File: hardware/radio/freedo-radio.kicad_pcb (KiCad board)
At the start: 4 copper layers, 92 x 60 mm, 146 parts, among them J1 SMA-KE-347-H13.5-1.6, J201 TYPE-C-31-M-12, J202 UART0, J301 DS1128-S80BP, SW201 TS-1187A-B-A-B, SW202 TS-1187A-B-A-B, T301 B1608S, U1 CC1101RGPR, U201 ESP32-S3-MINI-1-N8, U202 USBLC6-2SC6, U203 LDL1117S33R, U301 W5500, U401 DP9900LP-5V, X1 X322526MMB4SI, Y301 X322525MOB4SI

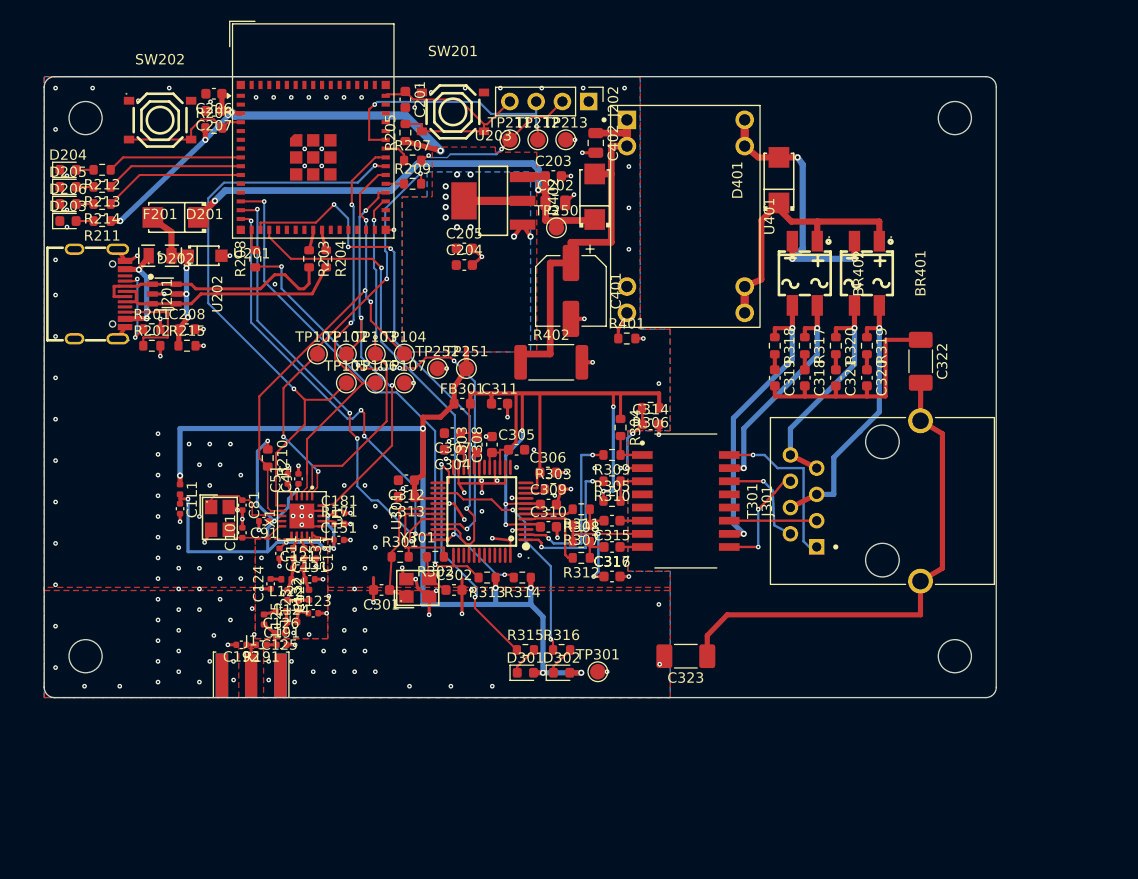
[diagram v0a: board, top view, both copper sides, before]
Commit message: fix(hardware): apply the pcb review fixes and align the usb-c to the edge
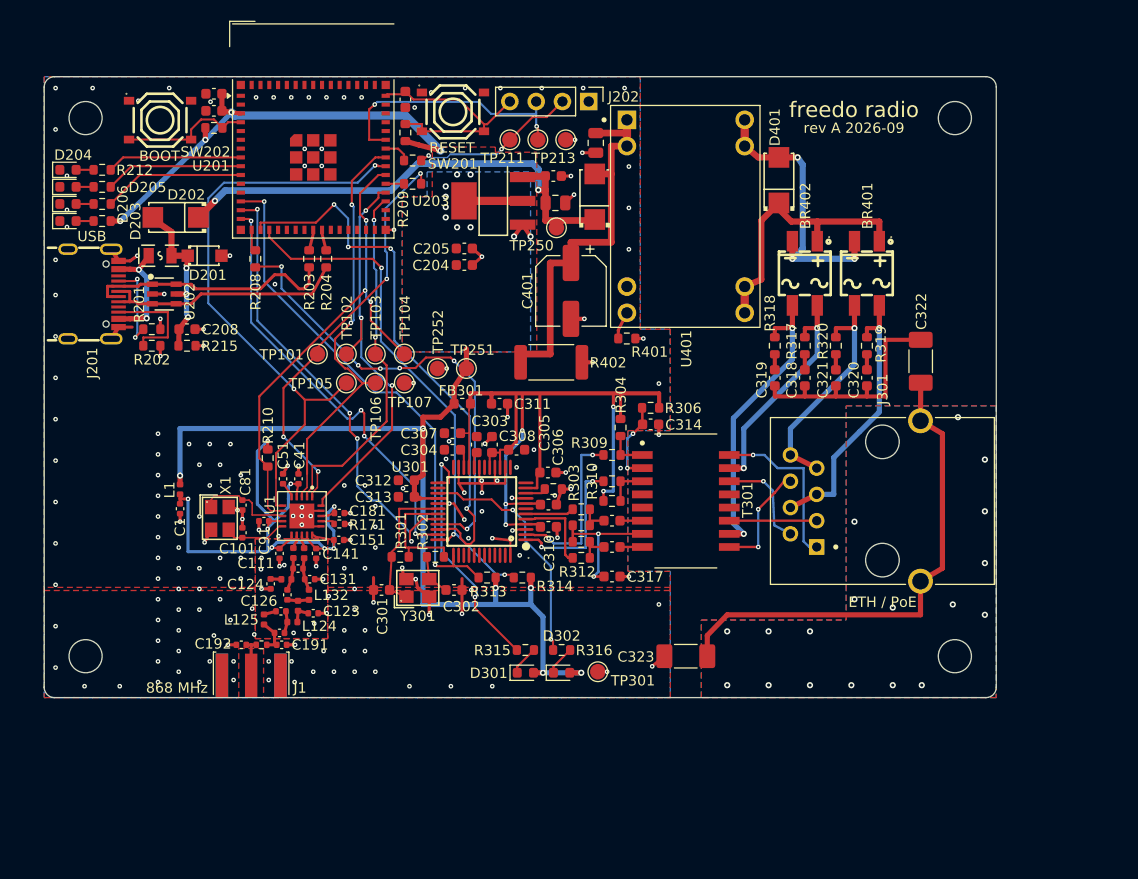
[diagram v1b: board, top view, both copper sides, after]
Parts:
- moved J201 0.63 mm to (194.8, 71.0)
- moved C51 0.45 mm to (213.1, 88.9)
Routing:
- net /rf/3V3_RF: track 52.3 -> 56.7 mm
- net GND: track 73.9 -> 78.0 mm, vias 197 -> 200
- net Net-(F201-Pad1): track 9.11 -> 10.4 mm
- net /usb_power/USB_DP: track 22.6 -> 23.2 mm
- net /usb_power/CC2: track 8.87 -> 9.50 mm
- net /usb_power/CC1: track 7.58 -> 8.21 mm
- net /usb_power/USB_DN: track 22.6 -> 23.2 mm
- net /ethernet_poe/SHIELD: vias 0 -> 18
- added copper zone on B.Cu, net /ethernet_poe/SHIELD
- added copper zone on F.Cu, net /ethernet_poe/SHIELD
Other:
- board text added: "868 MHz"
- board text added: "BOOT"
- board text added: "ETH / PoE"
- board text added: "RESET"
- board text added: "USB"
- board text added: "freedo radio"
- board text added: "rev A 2026-09"

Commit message: feat(hardware): re-place the board with rework spacing
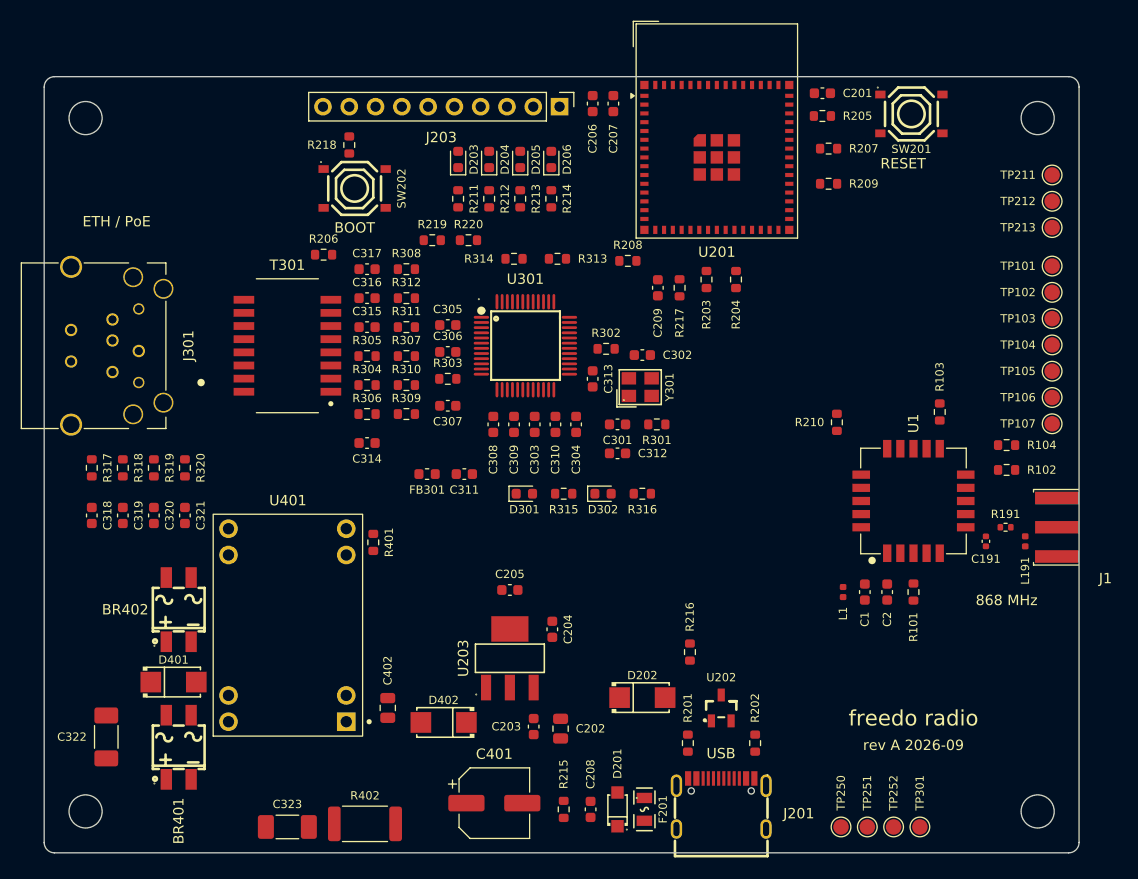
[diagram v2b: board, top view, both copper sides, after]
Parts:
- removed C101, C81: 15pF, freedo-radio:C_0402_1005Metric
- removed C111, C141, C151, C181, C41, C51, C91: 100nF, freedo-radio:C_0402_1005Metric
- removed C121: 1pF, freedo-radio:C_0402_1005Metric
- removed C122, C131: 1.5pF, freedo-radio:C_0402_1005Metric
- removed C123: 3.3pF, freedo-radio:C_0402_1005Metric
- removed C124: 100pF, freedo-radio:C_0402_1005Metric
- removed C125: 12pF, freedo-radio:C_0402_1005Metric
- removed C126: 47pF, freedo-radio:C_0402_1005Metric
- removed C192: DNP, freedo-radio:C_0402_1005Metric
- removed J202: UART0, freedo-radio:PinHeader_1x04_P2.54mm_Vertical
- removed L121, L123, L124, L131: 12nH, freedo-radio:L_0402_1005Metric
- removed L122, L132: 18nH, freedo-radio:L_0402_1005Metric
- removed L125: 3.3nH, freedo-radio:L_0402_1005Metric
- removed R171: 56k, freedo-radio:R_0402_1005Metric
- removed X1: X322526MMB4SI, freedo-radio:CRYSTAL-SMD_4P-L3.2-W2.5-BL
- added C2: 100nF, freedo-radio:C_0603_1608Metric, F.Cu at (271.5, 99.8)
- added C209: 100nF, freedo-radio:C_0603_1608Metric, F.Cu at (249.3, 70.4)
- added J203: GPIO, freedo-radio:PinHeader_1x10_P2.54mm_Vertical, F.Cu at (239.8, 52.9)
- added L191: 56nH, freedo-radio:L_0402_1005Metric, F.Cu at (284.8, 94.9)
- added R101: 0R, freedo-radio:R_0603_1608Metric, F.Cu at (274.0, 99.8)
- added R102: 0R, freedo-radio:R_0603_1608Metric, F.Cu at (283.0, 88.0)
- added R103: 0R, freedo-radio:R_0603_1608Metric, F.Cu at (276.5, 82.4)
- added R104: 0R, freedo-radio:R_0603_1608Metric, F.Cu at (283.0, 85.6)
- added R216: 68k, freedo-radio:R_0603_1608Metric, F.Cu at (252.4, 105.6)
- added R217: 100k, freedo-radio:R_0603_1608Metric, F.Cu at (251.4, 70.4)
- added R218: 1k, freedo-radio:R_0603_1608Metric, F.Cu at (219.5, 56.6)
- added R219: 4.7k, freedo-radio:R_0603_1608Metric, F.Cu at (227.5, 65.8)
- added R220: 4.7k, freedo-radio:R_0603_1608Metric, F.Cu at (231.0, 65.8)
- C1: value 1uF -> 10uF; footprint freedo-radio:C_0402_1005Metric -> freedo-radio:C_0603_1608Metric
- C202: value 22uF -> 10uF
- D201: value SMF5.0A -> SMF6.0A
- J301: value DS1128-S80BP -> TM24RSG-5A-88; footprint freedo-radio:RJ45_CONNFLY_DS1128-S80BP -> freedo-radio:RJ45_Hirose_TM24RSG-5A-88
- R207: value 510R -> 1k
- R215: value 10k -> 4.7k
- U1: value CC1101RGPR -> E07-900MM10S; footprint freedo-radio:QFN-20-1EP_4x4mm_P0.5mm_EP2.4x2.4mm_TI_RGP0020H -> freedo-radio:Ebyte_LCC-20_10x10mm_P1.27mm_E07-MM10S_E22-MM22S
- U202: value USBLC6-2SC6 -> H5VUT2U; footprint freedo-radio:SOT-23-6_L2.9-W1.6-P0.95-LS2.8-BL -> freedo-radio:SOT-23-3_L2.9-W1.5-P1.90-LS2.6-BR
- U203: value LDL1117S33R -> TLV76133DCYR
- moved C322 86.7 mm to (196.0, 113.8)
- moved BR401 80.7 mm to (203.0, 114.8), turned to 90 degrees
- moved J1 79.2 mm to (287.9, 93.5), turned to 90 degrees
- moved J201 78.1 mm to (255.4, 120.2), turned to 0 degrees
- moved D401 76.0 mm to (202.5, 108.5), turned to 0 degrees
- moved J301 72.9 mm to (197.1, 76.0), turned to -90 degrees
- moved R191 72.8 mm to (282.9, 93.5), turned to 0 degrees
- moved TP101 71.5 mm to (287.4, 68.3)
- moved F201 71.1 mm to (248.0, 120.8), turned to -90 degrees
- moved C318 70.2 mm to (194.6, 92.4), turned to 90 degrees
- moved C320 70.2 mm to (200.6, 92.4), turned to 90 degrees
- moved R317 69.9 mm to (194.6, 87.8), turned to 90 degrees
- moved R319 69.9 mm to (200.6, 87.8), turned to 90 degrees
- moved R202 69.8 mm to (258.7, 114.4), turned to 90 degrees
- moved C191 68.8 mm to (281.0, 94.9), turned to 90 degrees
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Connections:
- net Net-(J1-In) renamed /rf/RF_J1
- C191 pad 1: Net-(C125-Pad2) -> /rf/RF_ANT
- R191 pad 1: Net-(C125-Pad2) -> /rf/RF_ANT
- U1 pad 1: /mcu/CC_SCK -> /rf/3V3_RF
- U1 pad 10: Net-(U1-XOSC_Q2) -> /rf/E22_RXEN_PAD10
- U1 pad 11: /rf/3V3_RF -> /rf/E22_BUSY_PAD11
- U1 pad 12: /rf/RF_P -> /mcu/CC_MISO
- U1 pad 13: /rf/RF_N -> /mcu/CC_MOSI
- U1 pad 14: /rf/3V3_RF -> /mcu/CC_CSN
- U1 pad 15: /rf/3V3_RF -> /mcu/CC_SCK
- U1 pad 17: Net-(U1-RBIAS) -> unconnected-(U1-NC-Pad17)
- U1 pad 18: /rf/3V3_RF -> /mcu/CC_GDO0
- U1 pad 19: GND -> /rf/E22_DIO2_PAD19
- U1 pad 2: /mcu/CC_MISO -> GND
- U1 pad 20: /mcu/CC_MOSI -> /mcu/CC_GDO2
- U1 pad 3: /mcu/CC_GDO2 -> /rf/E22_NRST_PAD3
- U1 pad 4: /rf/3V3_RF -> unconnected-(U1-NC-Pad4)
- U1 pad 5: Net-(U1-DCOUPL) -> unconnected-(U1-NC-Pad5)
- U1 pad 6: /mcu/CC_GDO0 -> /rf/RF_ANT
- U1 pad 7: /mcu/CC_CSN -> GND
- U1 pad 8: Net-(U1-XOSC_Q1) -> unconnected-(U1-NC-Pad8)
- U1 pad 9: /rf/3V3_RF -> /rf/E22_TXEN_PAD9
- U201 pad 11: unconnected-(U201-IO7-Pad11) -> /mcu/IO7
- U201 pad 12: unconnected-(U201-IO8-Pad12) -> /mcu/IO8
- U201 pad 19: unconnected-(U201-IO15-Pad19) -> /mcu/I2C_SDA
- U201 pad 20: unconnected-(U201-IO16-Pad20) -> /mcu/I2C_SCL
- U201 pad 21: unconnected-(U201-IO17-Pad21) -> /mcu/VBUS_SENSE
- U201 pad 25: unconnected-(U201-IO21-Pad25) -> /mcu/E22_NRST
- U201 pad 27: unconnected-(U201-IO47-Pad27) -> /mcu/E22_RXEN
- U201 pad 30: unconnected-(U201-IO48-Pad30) -> /mcu/E22_BUSY
- U201 pad 5: unconnected-(U201-IO1-Pad5) -> /mcu/IO1
- U201 pad 6: unconnected-(U201-IO2-Pad6) -> /mcu/IO2
- U202 pad 2: GND -> /usb_power/USB_DP
- U202 pad 3: /usb_power/USB_DP -> GND
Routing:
- net +3V3: track 143.9 -> 0.00 mm, vias 18 -> 0
- net GND: track 78.0 -> 0.00 mm, vias 200 -> 0
- net /ethernet_poe/3V3A: track 77.3 -> 0.00 mm, vias 5 -> 0
- net /mcu/CC_GDO0: track 58.5 -> 0.00 mm, vias 2 -> 0
- net /rf/3V3_RF: track 56.7 -> 0.00 mm, vias 8 -> 0
- net /ethernet_poe/ETH_MISO: track 53.7 -> 0.00 mm, vias 4 -> 0
- net /ethernet_poe/ETH_RST: track 51.2 -> 0.00 mm, vias 2 -> 0
- net /ethernet_poe/ETH_INT: track 50.8 -> 0.00 mm, vias 3 -> 0
- net /ethernet_poe/5V_SYS: track 49.2 -> 0.00 mm, vias 2 -> 0
- net /ethernet_poe/SHIELD: track 48.3 -> 0.00 mm, vias 18 -> 0
- net /mcu/CC_CSN: track 47.6 -> 0.00 mm, vias 3 -> 0
- net /ethernet_poe/ETH_SCK: track 45.5 -> 0.00 mm, vias 6 -> 0
- net /ethernet_poe/ETH_CS: track 44.5 -> 0.00 mm, vias 4 -> 0
- net /ethernet_poe/ETH_MOSI: track 42.0 -> 0.00 mm, vias 4 -> 0
- net /mcu/CC_GDO2: track 40.5 -> 0.00 mm, vias 2 -> 0
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- removed copper zone on B.Cu, net +3V3
- removed copper zone on F.Cu, net +3V3
- removed copper zone on B.Cu, net /ethernet_poe/SHIELD
- removed copper zone on F.Cu, net /ethernet_poe/SHIELD
- removed copper zone on B.Cu, net GND
- removed copper zone on F.Cu, net GND
- removed copper zone on In1.Cu, net GND
- removed copper zone on In2.Cu, net GND
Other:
- board size 92 x 60 mm -> 100 x 75 mm
- board text added: "3V3 B.Cu to L1"
- board text added: "3V3 B.Cu to U201 pad 3"
- board text added: "3V3 pour to U301"
- board text added: "5V_SYS"
- board text added: "BARRIER 3 mm, no copper on any layer"
- board text added: "CT / pairs to bridges"
- board text added: "E22 links"
- board text added: "EN"
- board text added: "EN / RESET / UART"
- board text added: "ETHERNET"
- board text added: "GDO to U1 left side"
- board text added: "HEADER / LED / BOOT"
- board text added: "IO1/IO2"
- board text added: "IO7/IO8"
- board text added: "LINE SIDE (PoE)"
- board text added: "MCU"
- board text added: "MDI RX F.Cu"
- board text added: "MDI TX B.Cu"
- board text added: "MDI line side F.Cu"
- board text added: "POWER / USB"
- board text added: "RADIO"
- board text added: "RF feed 50R CPWG + via fence"
- board text added: "SDA/SCL B.Cu"
- board text added: "TEST POINTS"
- board text added: "TX/RX to J203, B.Cu under U201"
- board text added: "U203 3V3 F.Cu >= 4 cm2 (+ B.Cu >= 3 cm2, >= 8 vias)"
- board text added: "UART to TP211/TP212"
- board text added: "USB D+/D- 90R pair, F.Cu, no via"
- board text added: "VBUS"
- board text added: "VBUS_SENSE"
- board text added: "W5500 SPI x6, F.Cu"
- board text added: "radio SPI/GDO x6 + E22, F.Cu"
- board text added: "radio TP stubs, B.Cu"
- board text removed: "Barrier: no copper"
- board text removed: "Ethernet U301"
- board text removed: "Line side"
- board text removed: "MCU U201"
- board text removed: "MCU support"
- board text removed: "Power U203"
- board text removed: "RF U1 / J1"
- board text removed: "U201 antenna overhang"
- board text removed: "USB J201"

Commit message: feat(hardware): make both spi buses planar and move decoupling to its pins
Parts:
- moved R206 62.2 mm to (278.7, 59.6)
- moved SW202 59.2 mm to (278.7, 53.2)
- moved R210 12.2 mm to (271.0, 72.0), turned to 180 degrees
- moved R314 5.76 mm to (240.8, 69.6)
- moved C311 4.91 mm to (230.3, 83.5), turned to -90 degrees
- moved C312 4.61 mm to (242.7, 82.7), turned to -90 degrees
- moved SW201 3.13 mm to (270.7, 53.2)
- moved C307 1.70 mm to (229.0, 80.1)
- moved C303 1.25 mm to (236.4, 82.8)
- moved C304 1.25 mm to (240.4, 82.8)
- moved C308 1.25 mm to (232.4, 82.8)
- moved C309 1.25 mm to (234.4, 82.8)
- moved C310 1.25 mm to (238.4, 82.8)
- moved R303 1.10 mm to (229.0, 78.1)
- moved R208 1.05 mm to (246.3, 68.8), turned to 45 degrees
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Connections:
- R208 pad 2: Net-(U201-IO12) -> Net-(U201-IO13)
- U201 pad 14: /ethernet_poe/ETH_CS -> /ethernet_poe/ETH_INT
- U201 pad 16: Net-(U201-IO12) -> /ethernet_poe/ETH_MISO
- U201 pad 17: /ethernet_poe/ETH_MISO -> Net-(U201-IO13)
- U201 pad 18: /ethernet_poe/ETH_INT -> /ethernet_poe/ETH_CS
- U201 pad 32: unconnected-(U201-IO36-Pad32) -> /mcu/CC_GDO2
- U201 pad 33: /mcu/CC_MISO -> /mcu/CC_GDO0
- U201 pad 34: /mcu/CC_MOSI -> unconnected-(U201-IO38-Pad34)
- U201 pad 37: /mcu/CC_GDO0 -> /mcu/CC_MOSI
- U201 pad 38: /mcu/CC_GDO2 -> /mcu/CC_MISO
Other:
- board text added: "E22 NRST, F.Cu"
- board text added: "E22 links, B.Cu"
- board text added: "GPIO0 B.Cu under U201"
- board text added: "HEADER / LED"
- board text added: "RESET / BOOT"
- board text added: "W5500 SPI x6"
- board text added: "radio SPI/GDO x6, F.Cu"
- board text removed: "E22 links"
- board text removed: "EN / RESET / UART"
- board text removed: "HEADER / LED / BOOT"
- board text removed: "W5500 SPI x6, F.Cu"
- board text removed: "radio SPI/GDO x6 + E22, F.Cu"

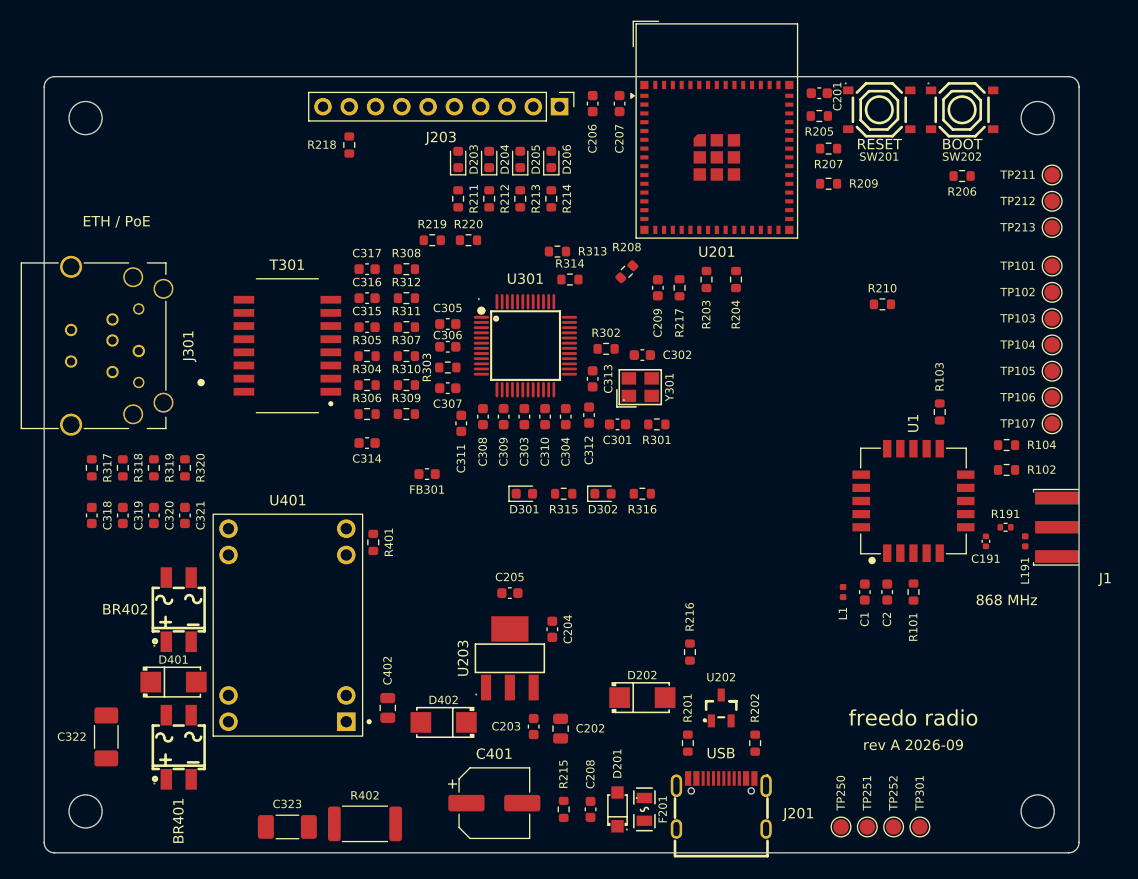
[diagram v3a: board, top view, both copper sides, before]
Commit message: feat(hardware): route the board with bus highways and solid ground planes
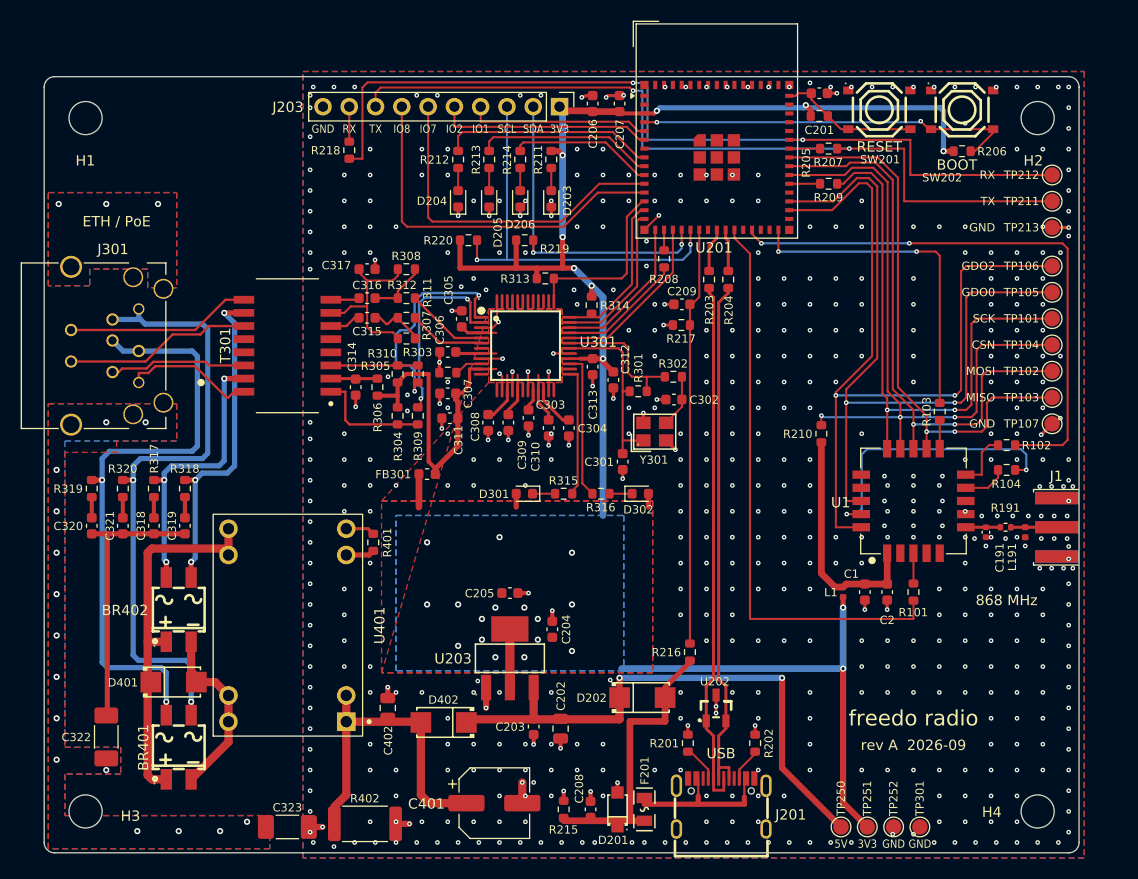
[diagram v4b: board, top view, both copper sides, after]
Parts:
- moved R210 13.8 mm to (265.1, 84.5), turned to 90 degrees
- moved TP106 12.7 mm to (287.4, 68.3)
- moved D203 9.77 mm to (239.0, 61.8)
- moved R211 9.77 mm to (239.0, 58.0), turned to -90 degrees
- moved R219 8.94 mm to (236.4, 65.8)
- moved TP103 7.62 mm to (287.4, 81.0)
- moved TP102 7.62 mm to (287.4, 78.5)
- moved TP105 7.62 mm to (287.4, 70.8)
- moved R302 7.04 mm to (250.8, 79.0)
- moved R317 6.32 mm to (200.6, 89.8), turned to -90 degrees
- moved R318 6.32 mm to (203.6, 89.8), turned to -90 degrees
- moved R319 6.32 mm to (194.6, 89.8), turned to -90 degrees
- moved R320 6.32 mm to (197.6, 89.8), turned to -90 degrees
- moved C318 6.08 mm to (200.6, 93.4), turned to -90 degrees
- moved C319 6.08 mm to (203.6, 93.4), turned to -90 degrees
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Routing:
- net +3V3: track 0.00 -> 164.5 mm, vias 0 -> 26
- net /mcu/UART0_RX: track 0.00 -> 84.9 mm, vias 0 -> 2
- net /mcu/UART0_TX: track 0.00 -> 78.9 mm, vias 0 -> 2
- net /mcu/CC_GDO2: track 0.00 -> 78.7 mm, vias 0 -> 2
- net /mcu/CC_GDO0: track 0.00 -> 72.8 mm, vias 0 -> 2
- net /mcu/CC_CSN: track 0.00 -> 66.3 mm, vias 0 -> 3
- net GND: track 0.00 -> 62.3 mm, vias 0 -> 551
- net /ethernet_poe/PAIR_78: track 0.00 -> 59.9 mm, vias 0 -> 2
- net /ethernet_poe/PAIR_45: track 0.00 -> 58.6 mm, vias 0 -> 2
- net /mcu/E22_NRST: track 0.00 -> 55.8 mm
- net /mcu/CC_MOSI: track 0.00 -> 55.6 mm, vias 0 -> 2
- net /mcu/E22_RXEN: track 0.00 -> 55.3 mm, vias 0 -> 2
- net /mcu/CC_SCK: track 0.00 -> 55.2 mm, vias 0 -> 2
- net /ethernet_poe/5V_SYS: track 0.00 -> 54.3 mm, vias 0 -> 2
- net /ethernet_poe/3V3A: track 0.00 -> 53.7 mm
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- added copper zone on B.Cu, net +3V3
- added copper zone on F.Cu, net +3V3
- added copper zone on F.Cu, net /ethernet_poe/3V3A
- added copper zone on B.Cu, net /ethernet_poe/SHIELD
- added copper zone on F.Cu, net /ethernet_poe/SHIELD
- added copper zone on B.Cu, net GND
- added copper zone on F.Cu, net GND
- added copper zone on In1.Cu, net GND
- added copper zone on In2.Cu, net GND
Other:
- board text added: "3V3"
- board text added: "5V"
- board text added: "CSN"
- board text added: "GDO0"
- board text added: "GDO2"
- board text added: "GND"
- board text added: "IO1"
- board text added: "IO2"
- board text added: "IO7"
- board text added: "IO8"
- board text added: "MISO"
- board text added: "MOSI"
- board text added: "RX"
- board text added: "SCK"
- board text added: "SCL"
- board text added: "SDA"
- board text added: "TX"
